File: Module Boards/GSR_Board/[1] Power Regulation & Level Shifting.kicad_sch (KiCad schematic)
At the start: 25 parts, among them U5 TPS7A9401DSCR, U6 TXS0102DQER

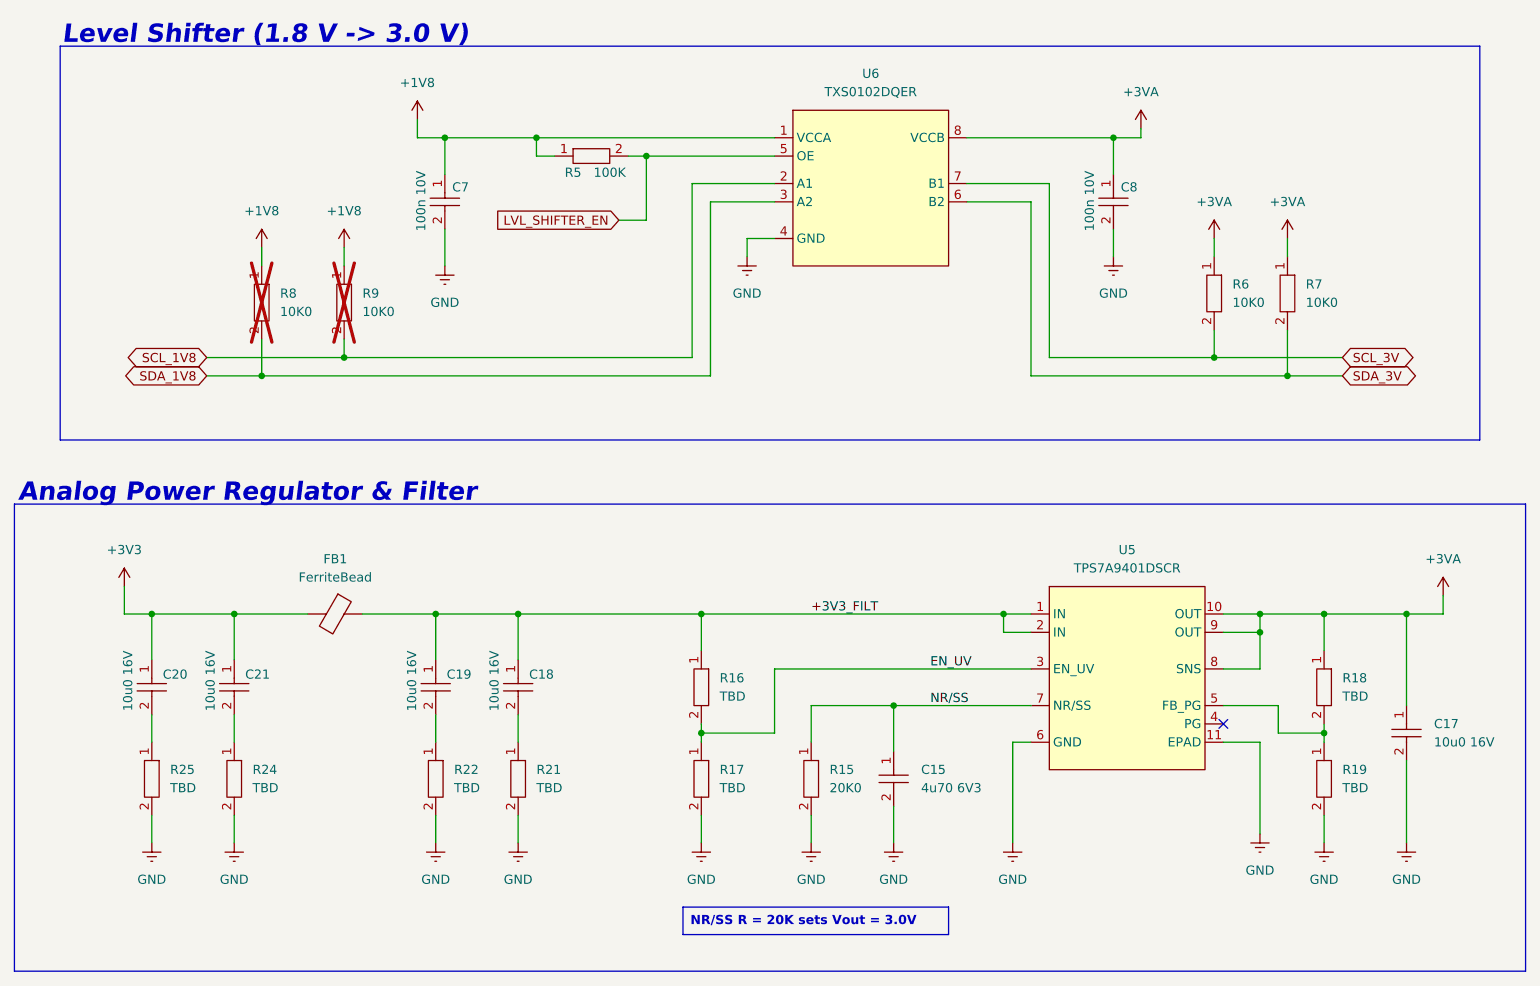
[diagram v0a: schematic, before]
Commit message: Added ADC to board and partially placed/routed the updated board
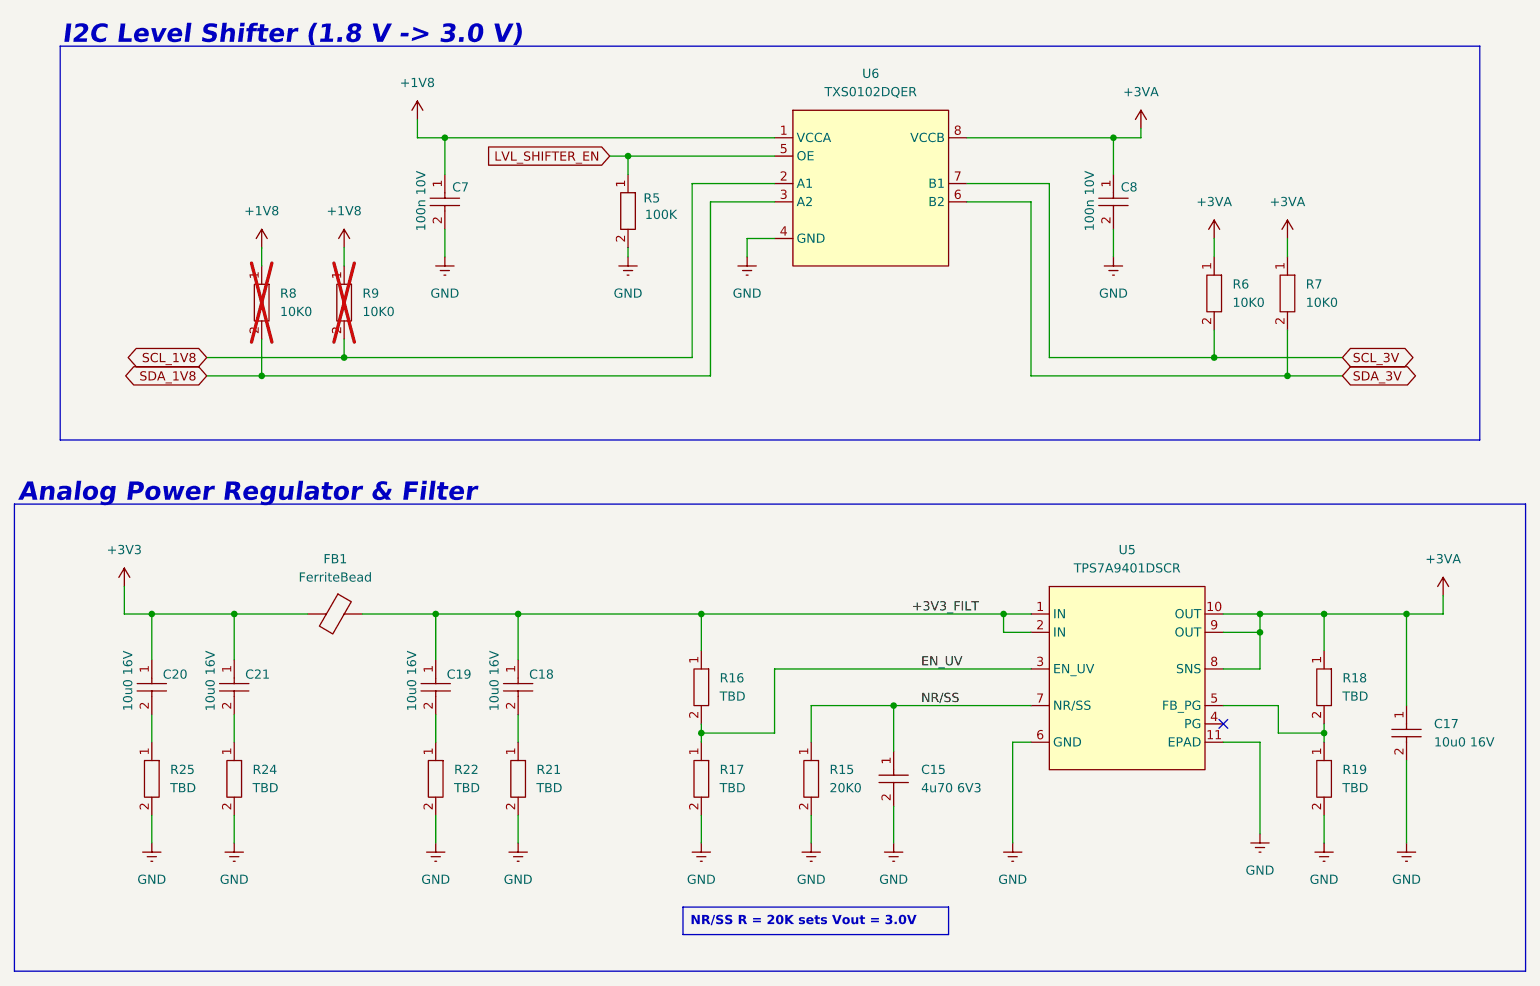
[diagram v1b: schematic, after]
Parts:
- U5: footprint X-MODs_PcbLib:WSON-8-3.15x3.15mm -> X-MODs_PcbLib:WSON-10-3.15x3.15mm
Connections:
- net +1V8: no longer R5.1
- net GND: now also R5.2
- net LVL_SHIFTER_EN: now also R5.1; no longer R5.2
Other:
- note added: "I2C Level Shifter (1.8 V -> 3.0 V)"
- note removed: "Level Shifter (1.8 V -> 3.0 V)"
- moved on the sheet: R5
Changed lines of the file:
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@@
 	)
 	(junction
-		(at 116.84 43.18)
+		(at 237.49 109.22)
 		(diameter 0)
 		(color 0 0 0 0)
 	)
 	(junction
-		(at 237.49 109.22)
+		(at 139.7 109.22)
 		(diameter 0)
 		(color 0 0 0 0)
 	)
 	(junction
-		(at 139.7 109.22)
+		(at 129.54 45.72)
 		(diameter 0)
 		(color 0 0 0 0)
@@
 	)
 	(junction
-		(at 132.08 45.72)
-		(diameter 0)
-		(color 0 0 0 0)
-	)
-	(junction
 		(at 78.74 76.2)
 		(diameter 0)
@@
 	(wire
 		(pts
+			(xy 127 45.72) (xy 129.54 45.72)
+		)
+		(stroke
+			(width 0)
+			(type default)
+		)
+	)
+	(wire
+		(pts
 			(xy 182.88 127) (xy 185.42 127)
 		)
@@
 	(wire
 		(pts
-			(xy 104.14 55.88) (xy 104.14 60.96)
+			(xy 104.14 55.88) (xy 104.14 59.69)
 		)
 		(stroke
@@
 	(wire
 		(pts
-			(xy 104.14 43.18) (xy 116.84 43.18)
+			(xy 104.14 43.18) (xy 149.86 43.18)
 		)
 		(stroke
@@
 	(wire
 		(pts
-			(xy 185.42 121.92) (xy 166.37 121.92)
-		)
-		(stroke
-			(width 0)
-			(type default)
-		)
-	)
-	(wire
-		(pts
 			(xy 114.3 123.19) (xy 114.3 127)
 		)
@@
 	(wire
 		(pts
-			(xy 116.84 45.72) (xy 116.84 43.18)
-		)
-		(stroke
-			(width 0)
-			(type default)
-		)
-	)
-	(wire
-		(pts
 			(xy 149.86 52.07) (xy 140.97 52.07)
 		)
@@
 	(wire
 		(pts
+			(xy 129.54 45.72) (xy 129.54 48.26)
+		)
+		(stroke
+			(width 0)
+			(type default)
+		)
+	)
+	(wire
+		(pts
 			(xy 149.86 116.84) (xy 149.86 125.73)
 		)
@@
 	(wire
 		(pts
+			(xy 129.54 58.42) (xy 129.54 59.69)
+		)
+		(stroke
+			(width 0)
+			(type default)
+		)
+	)
+	(wire
+		(pts
 			(xy 176.53 43.18) (xy 196.85 43.18)
 		)
@@
 	(wire
 		(pts
-			(xy 128.27 54.61) (xy 132.08 54.61)
+			(xy 129.54 45.72) (xy 149.86 45.72)
 		)
 		(stroke
@@
 	(wire
 		(pts
-			(xy 132.08 45.72) (xy 132.08 54.61)
-		)
-		(stroke
-			(width 0)
-			(type default)
-		)
-	)
-	(wire
-		(pts
 			(xy 226.06 124.46) (xy 226.06 125.73)
 		)
@@
 	(wire
 		(pts
-			(xy 129.54 45.72) (xy 132.08 45.72)
-		)
-		(stroke
-			(width 0)
-			(type default)
-		)
-	)
-	(wire
-		(pts
 			(xy 166.37 121.92) (xy 166.37 128.27)
 		)
@@
 	(wire
 		(pts
-			(xy 132.08 45.72) (xy 149.86 45.72)
-		)
-		(stroke
-			(width 0)
-			(type default)
-		)
-	)
-	(wire
-		(pts
 			(xy 212.09 121.92) (xy 219.71 121.92)
 		)
@@
 	(wire
 		(pts
-			(xy 119.38 45.72) (xy 116.84 45.72)
-		)
-		(stroke
-			(width 0)
-			(type default)
-		)
-	)
-	(wire
-		(pts
 			(xy 90.17 71.12) (xy 90.17 73.66)
 		)
@@
 	(wire
 		(pts
-			(xy 116.84 43.18) (xy 149.86 43.18)
-		)
-		(stroke
-			(width 0)
-			(type default)
-		)
-	)
-	(wire
-		(pts
 			(xy 196.85 43.18) (xy 200.66 43.18)
 		)
@@
 	(wire
 		(pts
+			(xy 166.37 121.92) (xy 185.42 121.92)
+		)
+		(stroke
+			(width 0)
+			(type default)
+		)
+	)
+	(wire
+		(pts
 			(xy 219.71 125.73) (xy 226.06 125.73)
 		)
@@
 		)
 	)
-	(text "Level Shifter (1.8 V -> 3.0 V)"
+	(text "I2C Level Shifter (1.8 V -> 3.0 V)"
 		(exclude_from_sim no)
 		(at 51.054 28.956 0)
@@
 	)
 	(label "EN_UV"
-		(at 171.45 116.84 0)
+		(at 170.18 116.84 0)
 		(fields_autoplaced yes)
 		(effects
@@
 	)
 	(label "+3V3_FILT"
-		(at 154.94 109.22 0)
+		(at 168.91 109.22 0)
 		(fields_autoplaced yes)
 		(effects
@@
 	)
 	(label "NR{slash}SS"
-		(at 171.45 121.92 0)
+		(at 170.18 121.92 0)
 		(fields_autoplaced yes)
 		(effects
@@
 	(global_label "LVL_SHIFTER_EN"
 		(shape input)
-		(at 128.27 54.61 180)
+		(at 127 45.72 180)
 		(fields_autoplaced yes)
 		(effects
@@
 		)
 		(property "Intersheetrefs" "${INTERSHEET_REFS}"
-			(at 110.1053 54.61 0)
+			(at 108.8353 45.72 0)
 			(effects
 				(font
@@
 	(symbol
 		(lib_id "power:Earth")
+		(at 129.54 59.69 0)
+		(unit 1)
+		(exclude_from_sim no)
+		(in_bom yes)
+		(on_board yes)
+		(dnp no)
+		(fields_autoplaced yes)
+		(property "Reference" "#PWR069"
+			(at 129.54 66.04 0)
+			(effects
+				(font
+					(size 1.27 1.27)
+				)
+				(hide yes)
+			)
+		)
+		(property "Value" "GND"
+			(at 129.54 64.77 0)
+			(effects
+				(font
+					(size 1.27 1.27)
+				)
+			)
+		)
+		(property "Footprint" ""
+			(at 129.54 59.69 0)
+			(effects
+				(font
+					(size 1.27 1.27)
+				)
+				(hide yes)
+			)
+		)
+		(property "Datasheet" "~"
+			(at 129.54 59.69 0)
+			(effects
+				(font
+					(size 1.27 1.27)
+				)
+				(hide yes)
+			)
+		)
+		(property "Description" "Power symbol creates a global label with name \"Earth\""
+			(at 129.54 59.69 0)
+			(effects
+				(font
+					(size 1.27 1.27)
+				)
+				(hide yes)
+			)
+		)
+		(pin "1"
+		)
+		(instances
+			(project "GSR_Board"
+				(path "/967fd416-113b-4abc-8322-5b19c6966929/37cd045a-36db-4748-ae75-68f8cec60c2f"
+					(reference "#PWR069")
+					(unit 1)
+				)
+			)
+		)
+	)
+	(symbol
+		(lib_id "power:Earth")
 		(at 182.88 140.97 0)
 		(unit 1)
@@
 	(symbol
 		(lib_id "X-MODs_SchLib:CRCW0402100KFKEDC")
-		(at 124.46 45.72 0)
+		(at 129.54 53.34 270)
 		(unit 1)
 		(exclude_from_sim no)
@@
 		(dnp no)
 		(property "Reference" "R5"
-			(at 121.92 48.006 0)
+			(at 132.842 51.562 90)
 			(effects
 				(font
@@
 		)
 		(property "Value" "100K"
-			(at 127 48.006 0)
+			(at 134.112 53.848 90)
 			(effects
 				(font
@@
 		)
 		(property "Footprint" "X-MODs_PcbLib:R0402"
-			(at 109.474 49.022 0)
+			(at 126.238 38.354 0)
 			(effects
 				(font
@@
 		)
 		(property "Datasheet" "https://www.vishay.com/doc?28773"
-			(at 109.474 52.832 0)
+			(at 122.428 38.354 0)
 			(effects
 				(font
@@
 		)
 		(property "Description" "Thick Film Resistors - SMD 1/16watt 100Kohms 1% Commercial Use"
-			(at 108.712 51.054 0)
+			(at 124.206 37.592 0)
 			(effects
 				(font
@@
 	(symbol
 		(lib_id "power:Earth")
-		(at 104.14 60.96 0)
+		(at 104.14 59.69 0)
 		(unit 1)
 		(exclude_from_sim no)
@@
 		(fields_autoplaced yes)
 		(property "Reference" "#PWR016"
-			(at 104.14 67.31 0)
+			(at 104.14 66.04 0)
 			(effects
 				(font
@@
 		)
 		(property "Value" "GND"
-			(at 104.14 66.04 0)
+			(at 104.14 64.77 0)
 			(effects
 				(font
@@
 		)
 		(property "Footprint" ""
-			(at 104.14 60.96 0)
+			(at 104.14 59.69 0)
 			(effects
 				(font
@@
 		)
 		(property "Datasheet" "~"
-			(at 104.14 60.96 0)
+			(at 104.14 59.69 0)
 			(effects
 				(font
@@
 		)
 		(property "Description" "Power symbol creates a global label with name \"Earth\""
-			(at 104.14 60.96 0)
+			(at 104.14 59.69 0)
 			(effects
 				(font
@@
 			)
 		)
-		(property "Footprint" "X-MODs_PcbLib:WSON-8-3.15x3.15mm"
+		(property "Footprint" "X-MODs_PcbLib:WSON-10-3.15x3.15mm"
 			(at 167.386 138.938 0)
 			(effects

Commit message: Finished Routing of GSR Board
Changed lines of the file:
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@@
 	(text "I2C Level Shifter (1.8 V -> 3.0 V)"
 		(exclude_from_sim no)
-		(at 51.054 28.956 0)
+		(at 51.308 29.21 0)
 		(effects
 			(font
@@
 	(text "Analog Power Regulator & Filter"
 		(exclude_from_sim no)
-		(at 44.958 92.456 0)
+		(at 44.958 92.71 0)
 		(effects
 			(font
